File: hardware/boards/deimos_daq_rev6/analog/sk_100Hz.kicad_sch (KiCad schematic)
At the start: 9 parts, among them U20002 OPA196xDBV

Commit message: move clamp diodes in schematic for filters. Add pulldown on ktype amp.
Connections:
- net VIN: now also D20002.2 (A)
- net at C15007.1, R15004.1, R15006.2: no longer D20002.2 (A)
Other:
- note added: "OVP diodes must be in front of filter resistors in order to prevent voltage error due to leakage current through the diode below breakdown voltage."
- moved on the sheet: D20001, D20002
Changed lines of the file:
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@@
-	)
-	(junction
-		(at 86.614 82.55)
-		(diameter 0)
-		(color 0 0 0 0)
 	)
 	(junction
@@
 	(wire
 		(pts
-			(xy 85.09 82.55) (xy 86.614 82.55)
+			(xy 85.09 82.55) (xy 88.9 82.55)
 		)
 		(stroke
@@
 		)
 	)
-	(wire
-		(pts
-			(xy 86.614 82.55) (xy 88.9 82.55)
-		)
-		(stroke
-			(width 0)
-			(type default)
+	(text "OVP diodes must be in front of\nfilter resistors in order to\nprevent voltage error due to\nleakage current through the\ndiode below breakdown voltage."
+		(exclude_from_sim no)
+		(at 63.5 109.728 0)
+		(effects
+			(font
+				(size 1.27 1.27)
+			)
+			(justify left)
 		)
 	)
@@
 	(symbol
 		(lib_id "Device:D_Zener")
-		(at 86.614 93.98 270)
+		(at 80.01 93.98 270)
 		(unit 1)
 		(exclude_from_sim no)
@@
 		(dnp no)
 		(property "Reference" "D20001"
-			(at 92.456 92.202 90)
+			(at 85.852 92.202 90)
 			(effects
 				(font
@@
 		)
 		(property "Value" "MMZ3Z3V3"
-			(at 93.726 93.98 90)
+			(at 87.122 93.98 90)
 			(effects
 				(font
@@
 		)
 		(property "Footprint" "Diode_SMD:D_SOD-323"
-			(at 86.614 93.98 0)
+			(at 80.01 93.98 0)
 			(effects
 				(font
@@
 		)
 		(property "Datasheet" "~"
-			(at 86.614 93.98 0)
+			(at 80.01 93.98 0)
 			(effects
 				(font
@@
 		)
 		(property "Description" ""
-			(at 86.614 93.98 0)
+			(at 80.01 93.98 0)
 			(effects
 				(font
@@
 		)
 		(property "LCSC" "C52056"
-			(at 86.614 93.98 0)
+			(at 80.01 93.98 0)
 			(effects
 				(font
@@
 	(symbol
 		(lib_id "power:GND")
-		(at 86.614 97.79 0)
+		(at 80.01 97.79 0)
 		(unit 1)
 		(exclude_from_sim no)
@@
 		(dnp no)
 		(property "Reference" "#PWR20005"
-			(at 86.614 104.14 0)
+			(at 80.01 104.14 0)
 			(effects
 				(font
@@
 		)
 		(property "Value" "GND"
-			(at 88.392 101.854 0)
+			(at 81.788 101.854 0)
 			(effects
 				(font
@@
 		)
 		(property "Footprint" ""
-			(at 86.614 97.79 0)
+			(at 80.01 97.79 0)
 			(effects
 				(font
@@
 		)
 		(property "Datasheet" ""
-			(at 86.614 97.79 0)
+			(at 80.01 97.79 0)
 			(effects
 				(font
@@
 		)
 		(property "Description" ""
-			(at 86.614 97.79 0)
+			(at 80.01 97.79 0)
 			(effects
 				(font
@@
 	(symbol
 		(lib_id "Device:D_Zener")
-		(at 86.614 86.36 90)
+		(at 80.01 86.36 90)
 		(unit 1)
 		(exclude_from_sim no)
@@
 		(dnp no)
 		(property "Reference" "D20002"
-			(at 80.772 88.138 90)
+			(at 74.168 88.138 90)
 			(effects
 				(font
@@
 		)
 		(property "Value" "MMZ3Z3V3"
-			(at 79.502 86.36 90)
+			(at 72.898 86.36 90)
 			(effects
 				(font
@@
 		)
 		(property "Footprint" "Diode_SMD:D_SOD-323"
-			(at 86.614 86.36 0)
+			(at 80.01 86.36 0)
 			(effects
 				(font
@@
 		)
 		(property "Datasheet" "~"
-			(at 86.614 86.36 0)
+			(at 80.01 86.36 0)
 			(effects
 				(font
@@
 		)
 		(property "Description" ""
-			(at 86.614 86.36 0)
+			(at 80.01 86.36 0)
 			(effects
 				(font
@@
 		)
 		(property "LCSC" "C52056"
-			(at 86.614 86.36 0)
-			(effects
-				(font
+			(at 80.01 86.36 0)
+			(effects
+				(font

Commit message: move ovp diodes behind filter amps. wip to implement 5V LDO.
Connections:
- net VIN: no longer D20002.2 (A)
- net VOUT: now also D20002.2 (A)
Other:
- note added: "OVP diodes must be outside filter resistors in order to prevent voltage error due to leakage current through the diode below breakdown voltage. For some channels that do not have an amplifier in front of the filter, diode leakage can still be an issue for accuracy due to resistors between the signal and the diodes. So, the only place left to put them that works consistently is after the filter op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"
- note removed: "OVP diodes must be in front of filter resistors in order to prevent voltage error due to leakage current through the diode below breakdown voltage."
- moved on the sheet: D20001, D20002
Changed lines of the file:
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@@
+	(wire
+		(pts
+			(xy 133.35 85.09) (xy 145.796 85.09)
+		)
+		(stroke
+			(width 0)
+			(type default)
+		)
+	)
 	(wire
 		(pts
@@
 		)
 	)
-	(text "OVP diodes must be in front of\nfilter resistors in order to\nprevent voltage error due to\nleakage current through the\ndiode below breakdown voltage."
-		(exclude_from_sim no)
-		(at 63.5 109.728 0)
+	(text "OVP diodes must be outside\nfilter resistors in order to\nprevent voltage error due to\nleakage current through the\ndiode below breakdown voltage.\n\nFor some channels that do not\nhave an amplifier in front of\nthe filter, diode leakage can\nstill be an issue for accuracy\ndue to resistors between the\nsignal and the diodes.\n\nSo, the only place left to put\nthem that works consistently is\nafter the filter opamp."
+		(exclude_from_sim no)
+		(at 170.942 107.95 0)
 		(effects
 			(font
@@
 	(hierarchical_label "VOUT"
 		(shape input)
-		(at 133.35 85.09 0)
+		(at 145.796 85.09 0)
 		(effects
 			(font
@@
 	(symbol
 		(lib_id "Device:D_Zener")
-		(at 80.01 93.98 270)
+		(at 145.796 96.52 270)
 		(unit 1)
 		(exclude_from_sim no)
@@
 		(dnp no)
 		(property "Reference" "D20001"
-			(at 85.852 92.202 90)
+			(at 151.638 94.742 90)
 			(effects
 				(font
@@
 		)
 		(property "Value" "MMZ3Z3V3"
-			(at 87.122 93.98 90)
+			(at 152.908 96.52 90)
 			(effects
 				(font
@@
 		)
 		(property "Footprint" "Diode_SMD:D_SOD-323"
-			(at 80.01 93.98 0)
+			(at 145.796 96.52 0)
 			(effects
 				(font
@@
 		)
 		(property "Datasheet" "~"
-			(at 80.01 93.98 0)
+			(at 145.796 96.52 0)
 			(effects
 				(font
@@
 		)
 		(property "Description" ""
-			(at 80.01 93.98 0)
+			(at 145.796 96.52 0)
 			(effects
 				(font
@@
 		)
 		(property "LCSC" "C52056"
-			(at 80.01 93.98 0)
+			(at 145.796 96.52 0)
 			(effects
 				(font
@@
 	(symbol
 		(lib_id "power:GND")
-		(at 80.01 97.79 0)
+		(at 145.796 100.33 0)
 		(unit 1)
 		(exclude_from_sim no)
@@
 		(dnp no)
 		(property "Reference" "#PWR20005"
-			(at 80.01 104.14 0)
+			(at 145.796 106.68 0)
 			(effects
 				(font
@@
 		)
 		(property "Value" "GND"
-			(at 81.788 101.854 0)
+			(at 147.574 104.394 0)
 			(effects
 				(font
@@
 		)
 		(property "Footprint" ""
-			(at 80.01 97.79 0)
+			(at 145.796 100.33 0)
 			(effects
 				(font
@@
 		)
 		(property "Datasheet" ""
-			(at 80.01 97.79 0)
+			(at 145.796 100.33 0)
 			(effects
 				(font
@@
 		)
 		(property "Description" ""
-			(at 80.01 97.79 0)
+			(at 145.796 100.33 0)
 			(effects
 				(font
@@
 	(symbol
 		(lib_id "Device:D_Zener")
-		(at 80.01 86.36 90)
+		(at 145.796 88.9 90)
 		(unit 1)
 		(exclude_from_sim no)
@@
 		(dnp no)
 		(property "Reference" "D20002"
-			(at 74.168 88.138 90)
+			(at 139.954 90.678 90)
 			(effects
 				(font
@@
 		)
 		(property "Value" "MMZ3Z3V3"
-			(at 72.898 86.36 90)
+			(at 138.684 88.9 90)
 			(effects
 				(font
@@
 		)
 		(property "Footprint" "Diode_SMD:D_SOD-323"
-			(at 80.01 86.36 0)
+			(at 145.796 88.9 0)
 			(effects
 				(font
@@
 		)
 		(property "Datasheet" "~"
-			(at 80.01 86.36 0)
+			(at 145.796 88.9 0)
 			(effects
 				(font
@@
 		)
 		(property "Description" ""
-			(at 80.01 86.36 0)
+			(at 145.796 88.9 0)
 			(effects
 				(font
@@
 		)
 		(property "LCSC" "C52056"
-			(at 80.01 86.36 0)
-			(effects
-				(font
+			(at 145.796 88.9 0)
+			(effects
+				(font

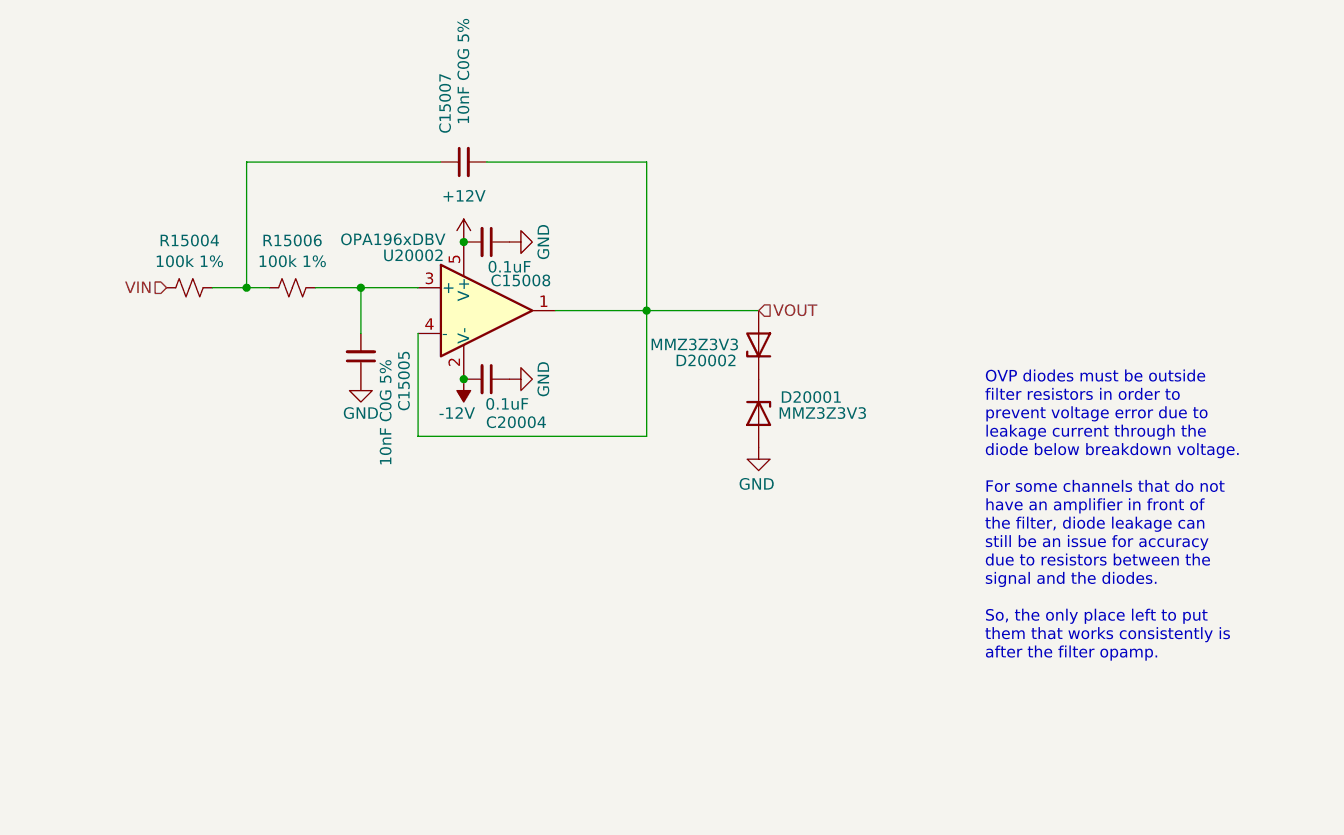
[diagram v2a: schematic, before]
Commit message: set up jfet diode clamps for filters
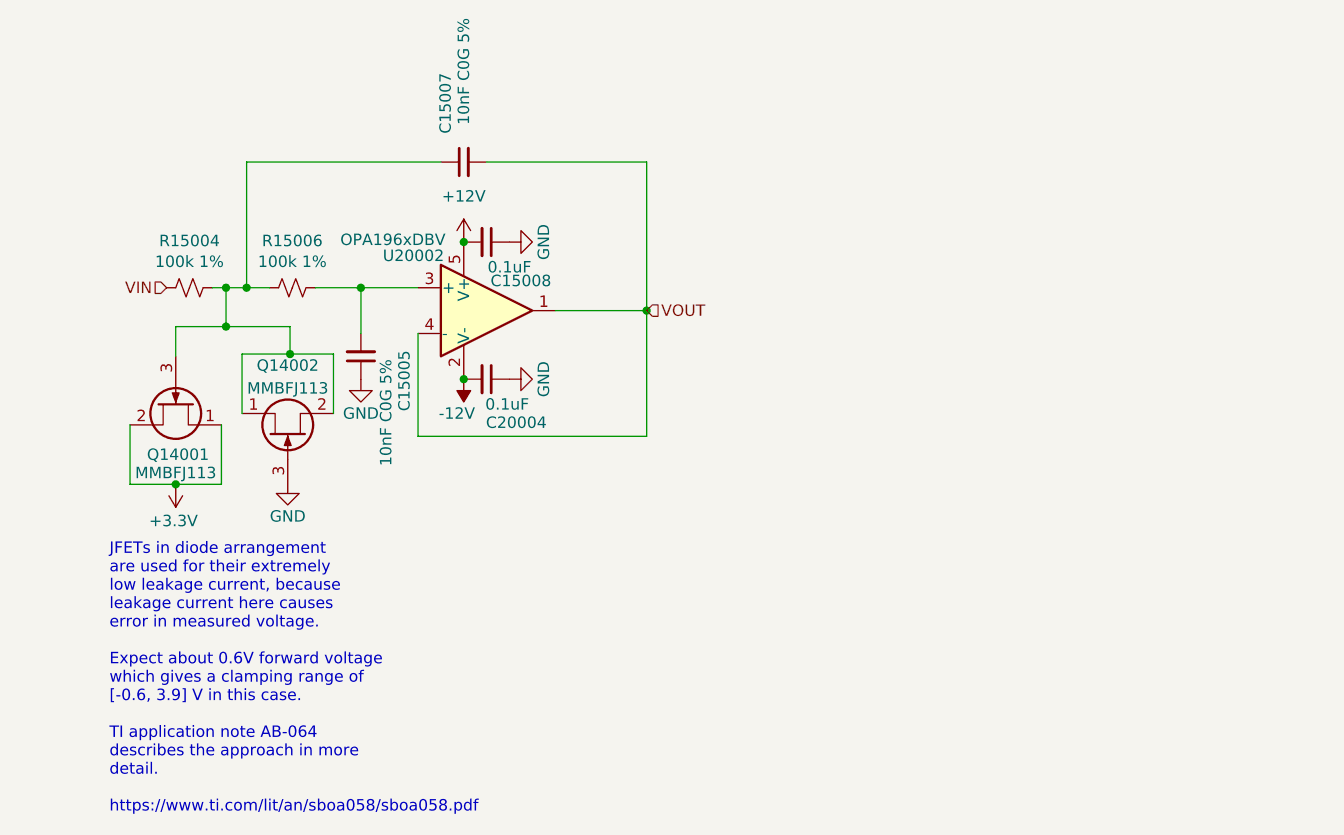
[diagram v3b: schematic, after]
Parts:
- removed D20001, D20002: MMZ3Z3V3, Diode_SMD:D_SOD-323, symbol Device:D_Zener
- added Q14001, Q14002: MMBFJ113, Package_TO_SOT_SMD:SOT-23, symbol Transistor_FET:MMBFJ113
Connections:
- net GND: now also Q14002.3 (G)
- net at C15007.1, R15004.1, R15006.2: now also Q14001.3 (G), Q14002.1 (D), Q14002.2 (S)
- new net +3.3V: Q14001.1 (D), Q14001.2 (S)
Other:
- note added: "JFETs in diode arrangement are used for their extremely low leakage current, because leakage current here causes error in measured voltage. Expect about 0.6V forward voltage which gives a clamping range of [-0.6, 3.9] V in this case. TI application note AB-064 describes the approach in more detail. https://www.ti.com/lit/an/sboa058/sboa058.pdf"
- note removed: "OVP diodes must be outside filter resistors in order to prevent voltage error due to leakage current through the diode below breakdown voltage. For some channels that do not have an amplifier in front of the filter, diode leakage can still be an issue for accuracy due to resistors between the signal and the diodes. So, the only place left to put them that works consistently is after the filter op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"

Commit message: wip to layout new voltage clamps
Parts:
- renumbered Q14001 to Q20001, Q14002 to Q20002
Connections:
- net +3.3V renamed +3V3
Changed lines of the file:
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@@
 	(paper "A4")
-	(junction
-		(at 81.026 104.394)
-		(diameter 0)
-		(color 0 0 0 0)
-	)
 	(junction
 		(at 113.03 92.71)
@@
 	)
 	(junction
+		(at 81.28 104.394)
+		(diameter 0)
+		(color 0 0 0 0)
+	)
+	(junction
 		(at 86.614 82.55)
 		(diameter 0)
@@
 	(wire
 		(pts
-			(xy 75.946 104.394) (xy 81.026 104.394)
+			(xy 75.946 104.394) (xy 81.28 104.394)
 		)
 		(stroke
@@
 	(wire
 		(pts
+			(xy 81.28 104.394) (xy 86.106 104.394)
+		)
+		(stroke
+			(width 0)
+			(type default)
+		)
+	)
+	(wire
+		(pts
 			(xy 88.392 89.916) (xy 93.726 89.916)
 		)
@@
 		(pts
 			(xy 96.52 82.55) (xy 101.6 82.55)
-		)
-		(stroke
-			(width 0)
-			(type default)
-		)
-	)
-	(wire
-		(pts
-			(xy 86.106 104.394) (xy 81.026 104.394)
 		)
 		(stroke
@@
 		(on_board yes)
 		(dnp no)
-		(property "Reference" "Q14001"
+		(property "Reference" "Q20001"
 			(at 81.28 101.092 90)
 			(effects
@@
 		(on_board yes)
 		(dnp no)
-		(property "Reference" "#PWR14007"
+		(property "Reference" "#PWR20007"
 			(at 93.472 110.49 0)
 			(effects
@@
 	)
 	(symbol
+		(lib_id "power:+3V3")
+		(at 81.28 104.394 180)
+		(unit 1)
+		(exclude_from_sim no)
+		(in_bom yes)
+		(on_board yes)
+		(dnp no)
+		(fields_autoplaced yes)
+		(property "Reference" "#PWR20005"
+			(at 81.28 100.584 0)
+			(effects
+				(font
+					(size 1.27 1.27)
+				)
+				(hide yes)
+			)
+		)
+		(property "Value" "+3V3"
+			(at 81.28 109.22 0)
+			(effects
+				(font
+					(size 1.27 1.27)
+				)
+			)
+		)
+		(property "Footprint" ""
+			(at 81.28 104.394 0)
+			(effects
+				(font
+					(size 1.27 1.27)
+				)
+				(hide yes)
+			)
+		)
+		(property "Datasheet" ""
+			(at 81.28 104.394 0)
+			(effects
+				(font
+					(size 1.27 1.27)
+				)
+				(hide yes)
+			)
+		)
+		(property "Description" "Power symbol creates a global label with name \"+3V3\""
+			(at 81.28 104.394 0)
+			(effects
+				(font
+					(size 1.27 1.27)
+				)
+				(hide yes)
+			)
+		)
+		(pin "1"
+		)
+		(instances
+			(project ""
+				(path "/c241d083-1323-4b4a-a540-956d0afb7b72/f31a785a-aa18-4b99-9461-7c34b37be0d7"
+					(reference "#PWR20005")
+					(unit 1)
+				)
+				(path "/c241d083-1323-4b4a-a540-956d0afb7b72/ed60502d-2e6d-4293-85f2-5e967a3c42d8/63cb4c21-96ec-4930-8398-5e4d00a3dfaf"
+					(reference "#PWR14005")
+					(unit 1)
+				)
+			)
+		)
+	)
+	(symbol
 		(lib_id "Device:R_Small_US")
 		(at 82.55 82.55 270)
@@
 		(on_board yes)
 		(dnp no)
-		(property "Reference" "Q14002"
+		(property "Reference" "Q20002"
 			(at 93.472 91.186 90)
 			(effects
@@
 					(unit 1)
 				)
-			)
-		)
-	)
-	(symbol
-		(lib_id "power:+3.3V")
-		(at 81.026 104.394 180)
-		(unit 1)
-		(exclude_from_sim no)
-		(in_bom yes)
-		(on_board yes)
-		(dnp no)
-		(property "Reference" "#PWR14005"
-			(at 81.026 100.584 0)
-			(effects
-				(font
-					(size 1.27 1.27)
-				)
-				(hide yes)
-			)
-		)
-		(property "Value" "+3.3V"
-			(at 80.772 108.458 0)
-			(effects
-				(font
-					(size 1.27 1.27)
-				)
-			)
-		)
-		(property "Footprint" ""
-			(at 81.026 104.394 0)
-			(effects
-				(font
-					(size 1.27 1.27)
-				)
-				(hide yes)
-			)
-		)
-		(property "Datasheet" ""
-			(at 81.026 104.394 0)
-			(effects
-				(font
-					(size 1.27 1.27)
-				)
-				(hide yes)
-			)
-		)
-		(property "Description" "Power symbol creates a global label with name \"+3.3V\""
-			(at 81.026 104.394 0)
-			(effects
-				(font
-					(size 1.27 1.27)
-				)
-				(hide yes)
-			)
-		)
-		(pin "1"
-		)
-		(instances
-			(project "analog_frontend_panel"
-				(path "/c241d083-1323-4b4a-a540-956d0afb7b72/f31a785a-aa18-4b99-9461-7c34b37be0d7"
-					(reference "#PWR20005")
-					(unit 1)
-				)
-				(path "/c241d083-1323-4b4a-a540-956d0afb7b72/ed60502d-2e6d-4293-85f2-5e967a3c42d8/63cb4c21-96ec-4930-8398-5e4d00a3dfaf"
-					(reference "#PWR14005")
-					(unit 1)
-				)
